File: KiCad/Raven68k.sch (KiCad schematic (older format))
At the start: 22 parts, among them CON1 BARREL_JACK, P1 CONN_01X06, U1 68000D, U2 28C256, U3 SRAM_512Ko, U4 SRAM_512Ko, U5 28C256, U6 XC9572XL-TQ100, U7 68681, Y1 Crystal_GND24

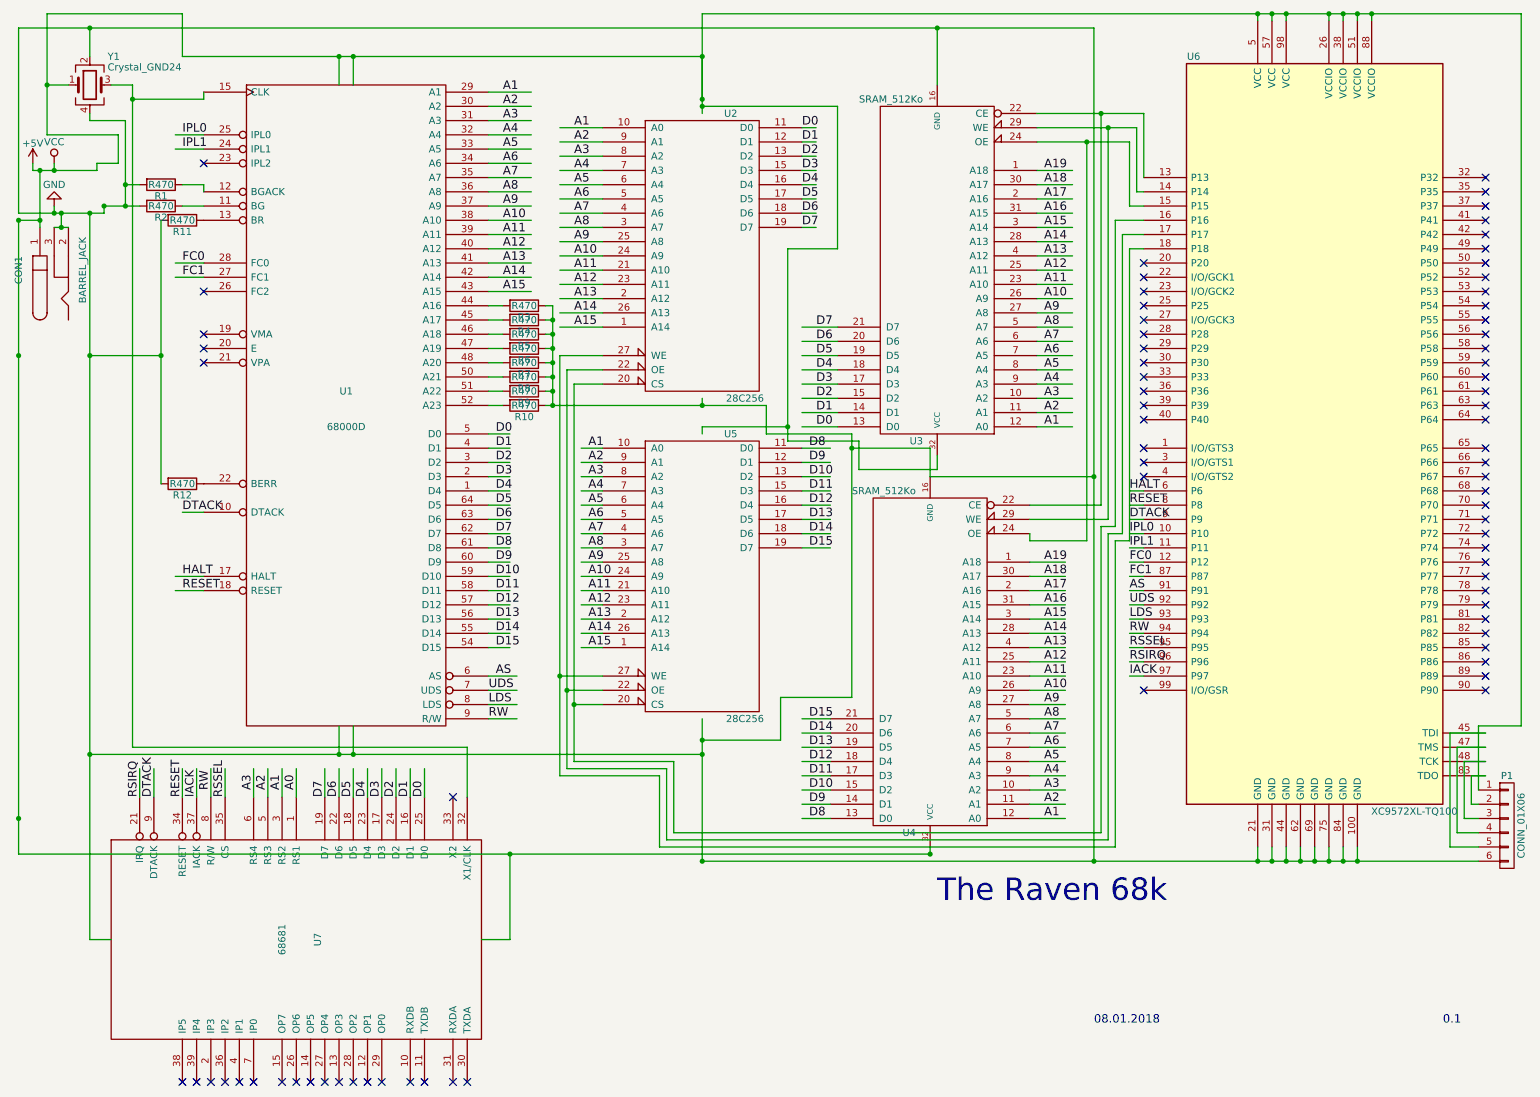
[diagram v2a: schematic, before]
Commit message: Fixed an issue with un-connected address pins a16..a19 and wrong address pin numbering on the RSx register select pins on the 68681.
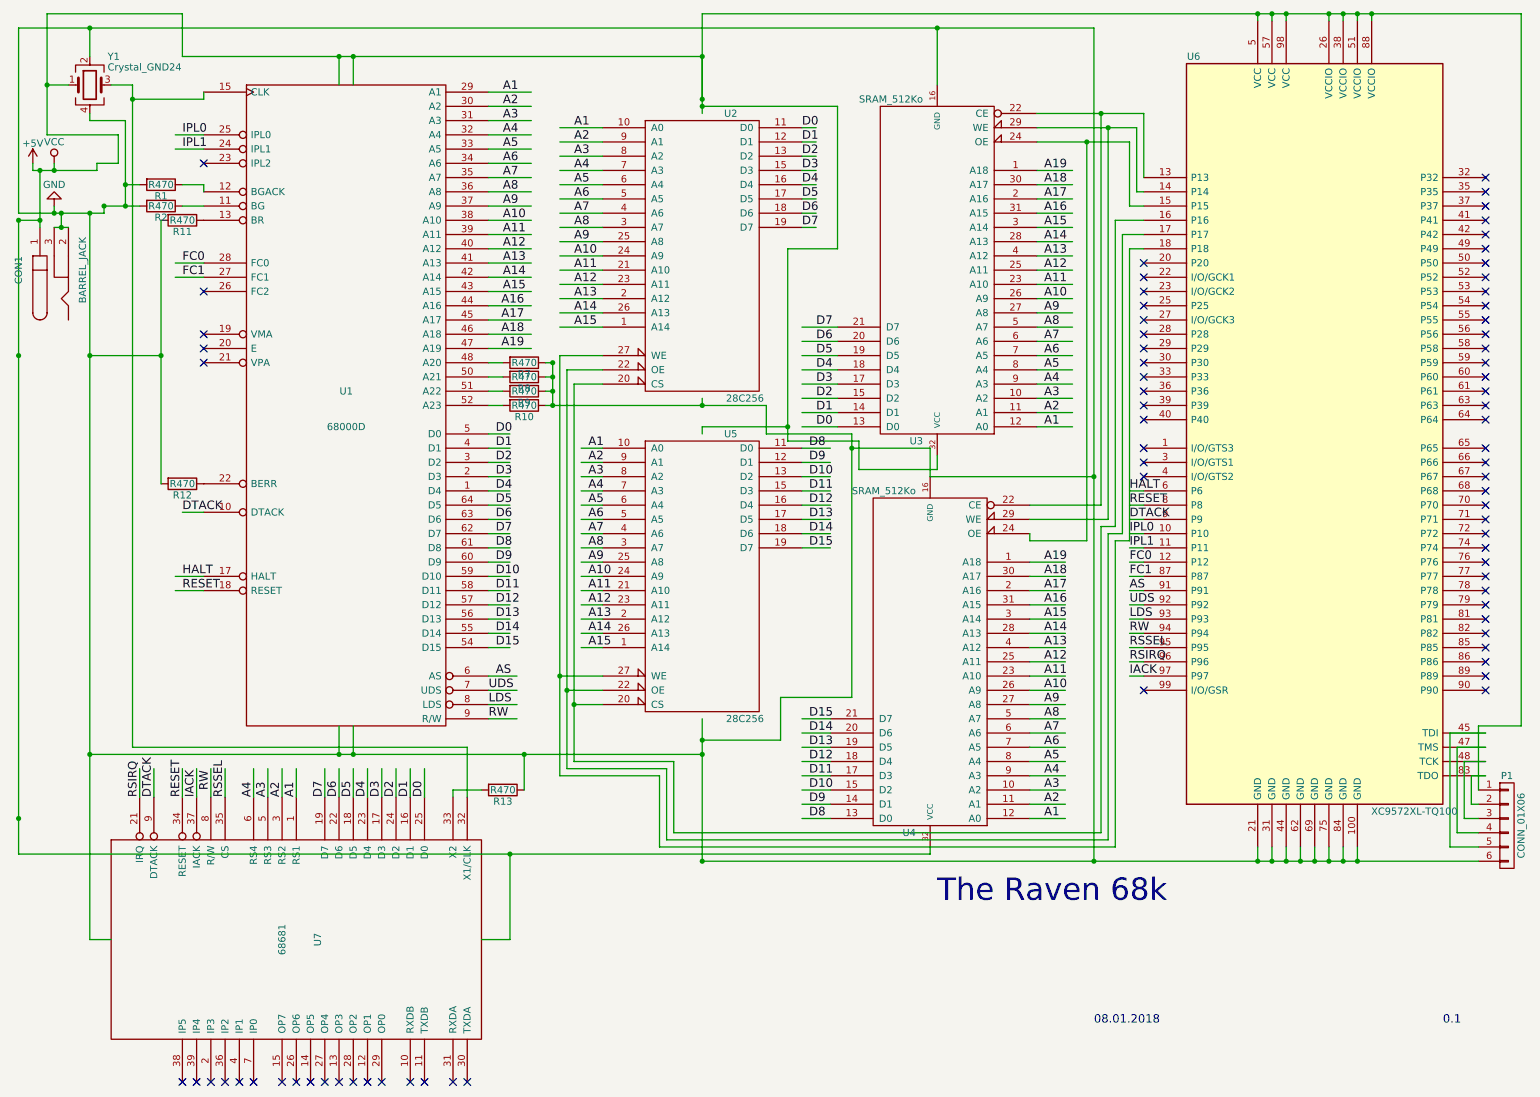
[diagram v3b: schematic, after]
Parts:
- removed R3, R4, R5, R6: R470, Resistors_Universal:Resistor_SMD+THTuniversal_1206_RM10_HandSoldering, symbol R
- added R13: R470, Resistors_Universal:Resistor_SMD+THTuniversal_1206_RM10_HandSoldering, symbol R
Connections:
- net labels removed: A0
- wire segments 343 -> 342
- no-connect marks 76 -> 75
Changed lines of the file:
@@
 FC1
-$Comp
-L R R3
-U 1 1 5A56B70B
-P 4150 2600
-F 0 "R3" V 4230 2600 50  0000 C CNN
-F 1 "R470" V 4150 2600 50  0000 C CNN
-F 2 "Resistors_Universal:Resistor_SMD+THTuniversal_1206_RM10_HandSoldering" V 4080 2600 50  0001 C CNN
-F 3 "" H 4150 2600 50  0000 C CNN
-	1    4150 2600
-	0    1    1    0
-$EndComp
-$Comp
-L R R4
-U 1 1 5A56B7AF
-P 4150 2700
-F 0 "R4" V 4230 2700 50  0000 C CNN
-F 1 "R470" V 4150 2700 50  0000 C CNN
-F 2 "Resistors_Universal:Resistor_SMD+THTuniversal_1206_RM10_HandSoldering" V 4080 2700 50  0001 C CNN
-F 3 "" H 4150 2700 50  0000 C CNN
-	1    4150 2700
-	0    1    1    0
-$EndComp
-$Comp
-L R R5
-U 1 1 5A56B7E6
-P 4150 2800
-F 0 "R5" V 4230 2800 50  0000 C CNN
-F 1 "R470" V 4150 2800 50  0000 C CNN
-F 2 "Resistors_Universal:Resistor_SMD+THTuniversal_1206_RM10_HandSoldering" V 4080 2800 50  0001 C CNN
-F 3 "" H 4150 2800 50  0000 C CNN
-	1    4150 2800
-	0    1    1    0
-$EndComp
-$Comp
-L R R6
-U 1 1 5A56B820
-P 4150 2900
-F 0 "R6" V 4230 2900 50  0000 C CNN
-F 1 "R470" V 4150 2900 50  0000 C CNN
-F 2 "Resistors_Universal:Resistor_SMD+THTuniversal_1206_RM10_HandSoldering" V 4080 2900 50  0001 C CNN
-F 3 "" H 4150 2900 50  0000 C CNN
-	1    4150 2900
-	0    1    1    0
-$EndComp
 $Comp
 L R R7
@@
 	1750 850  5400 850
 Wire Wire Line
-	2950 5750 2950 5550
-Connection ~ 2950 5750
-Wire Wire Line
 	5400 850  5400 1250
 Connection ~ 600  6200
@@
 	600  2000 600  6450
 Wire Wire Line
-	7000 6400 7000 6450
-Connection ~ 7000 6450
-Wire Wire Line
 	9900 6400 9900 6500
 Connection ~ 9900 6500
@@
 	9400 600  9400 550
 Connection ~ 9400 550
-Wire Wire Line
-	9300 600  9300 550
-Connection ~ 9300 550
 Wire Wire Line
 	10100 550  10100 600
@@
 	8500 4500 8400 4500
 Wire Wire Line
-	3900 2600 4000 2600
-Wire Wire Line
-	3900 2700 4000 2700
-Wire Wire Line
-	3900 2800 4000 2800
-Wire Wire Line
-	3900 2900 4000 2900
-Wire Wire Line
 	3900 3000 4000 3000
 Wire Wire Line
@@
 	3900 3300 4000 3300
 Wire Wire Line
-	4300 2600 4350 2600
-Wire Wire Line
 	4350 3200 4300 3200
 Wire Wire Line
@@
 	4350 3000 4300 3000
 Wire Wire Line
-	4350 2900 4300 2900
-Wire Wire Line
-	4350 2800 4300 2800
-Wire Wire Line
-	4300 2700 4350 2700
-Wire Wire Line
 	7700 4700 7950 4700
-Wire Wire Line
-	4350 2600 4350 3300
-Connection ~ 4350 2700
-Connection ~ 4350 2800
-Connection ~ 4350 2900
 Connection ~ 4350 3000
 Connection ~ 4350 3100
@@
 Connection ~ 8150 6500
 Wire Wire Line
-	7000 6450 600  6450
+	600  6450 7000 6450
 Wire Wire Line
 	5400 5500 5400 6500
@@
 Connection ~ 2850 5750
 Wire Wire Line
-	5400 3250 5400 3300
-Connection ~ 5400 3300
-Wire Wire Line
 	5400 3450 5400 3500
 Wire Wire Line
@@
 Wire Wire Line
 	6500 3750 7050 3750
-Wire Wire Line
-	7050 3750 7050 3650
 Wire Wire Line
 	850  1600 850  1650
@@
 Wire Wire Line
 	2250 6050 2250 5850
-Text Label 2550 6000 1    60   ~ 0
-A0
-Text Label 2450 6000 1    60   ~ 0
-A1
-Text Label 2350 6000 1    60   ~ 0
-A2
-Text Label 2250 6000 1    60   ~ 0
-A3
 Connection ~ 5400 6500
 Connection ~ 5400 5750
@@
 	3750 5700 3750 6050
 Connection ~ 1400 1150
-NoConn ~ 3650 6050
+$Comp
+L R R13
+U 1 1 5A5921D0
+P 4000 6000
+F 0 "R13" V 4080 6000 50  0000 C CNN
+F 1 "R470" V 4000 6000 50  0000 C CNN
+F 2 "Resistors_Universal:Resistor_SMD+THTuniversal_1206_RM10_HandSoldering" V 3930 6000 50  0001 C CNN
+F 3 "" H 4000 6000 50  0000 C CNN
+	1    4000 6000
+	0    1    1    0
+$EndComp
+Wire Wire Line
+	3650 6050 3650 6000
+Wire Wire Line
+	3650 6000 3850 6000
+Wire Wire Line
+	4150 6000 4150 5750
+Connection ~ 4150 5750
+Wire Wire Line
+	4350 3000 4350 3300
+Wire Wire Line
+	3900 2600 4200 2600
+Wire Wire Line
+	3900 2700 4200 2700
+Wire Wire Line
+	3900 2800 4200 2800
+Wire Wire Line
+	3900 2900 4200 2900
+Text Label 4150 2600 2    60   ~ 0
+A16
+Text Label 4150 2700 2    60   ~ 0
+A17
+Text Label 4150 2800 2    60   ~ 0
+A18
+Text Label 4150 2900 2    60   ~ 0
+A19
+Text Label 2550 6050 1    60   ~ 0
+A1
+Text Label 2450 6050 1    60   ~ 0
+A2
+Text Label 2350 6050 1    60   ~ 0
+A3
+Text Label 2250 6050 1    60   ~ 0
+A4
+Wire Wire Line
+	7050 3750 7050 3650
+Wire Wire Line
+	7000 6450 7000 6400
+Wire Wire Line
+	2950 5550 2950 5750
+Connection ~ 2950 5750
+Wire Wire Line
+	9300 600  9300 550
+Connection ~ 9300 550
+Wire Wire Line
+	5400 3250 5400 3300
+Connection ~ 5400 3300
 $EndSCHEMATC

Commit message: hierarchial sheets
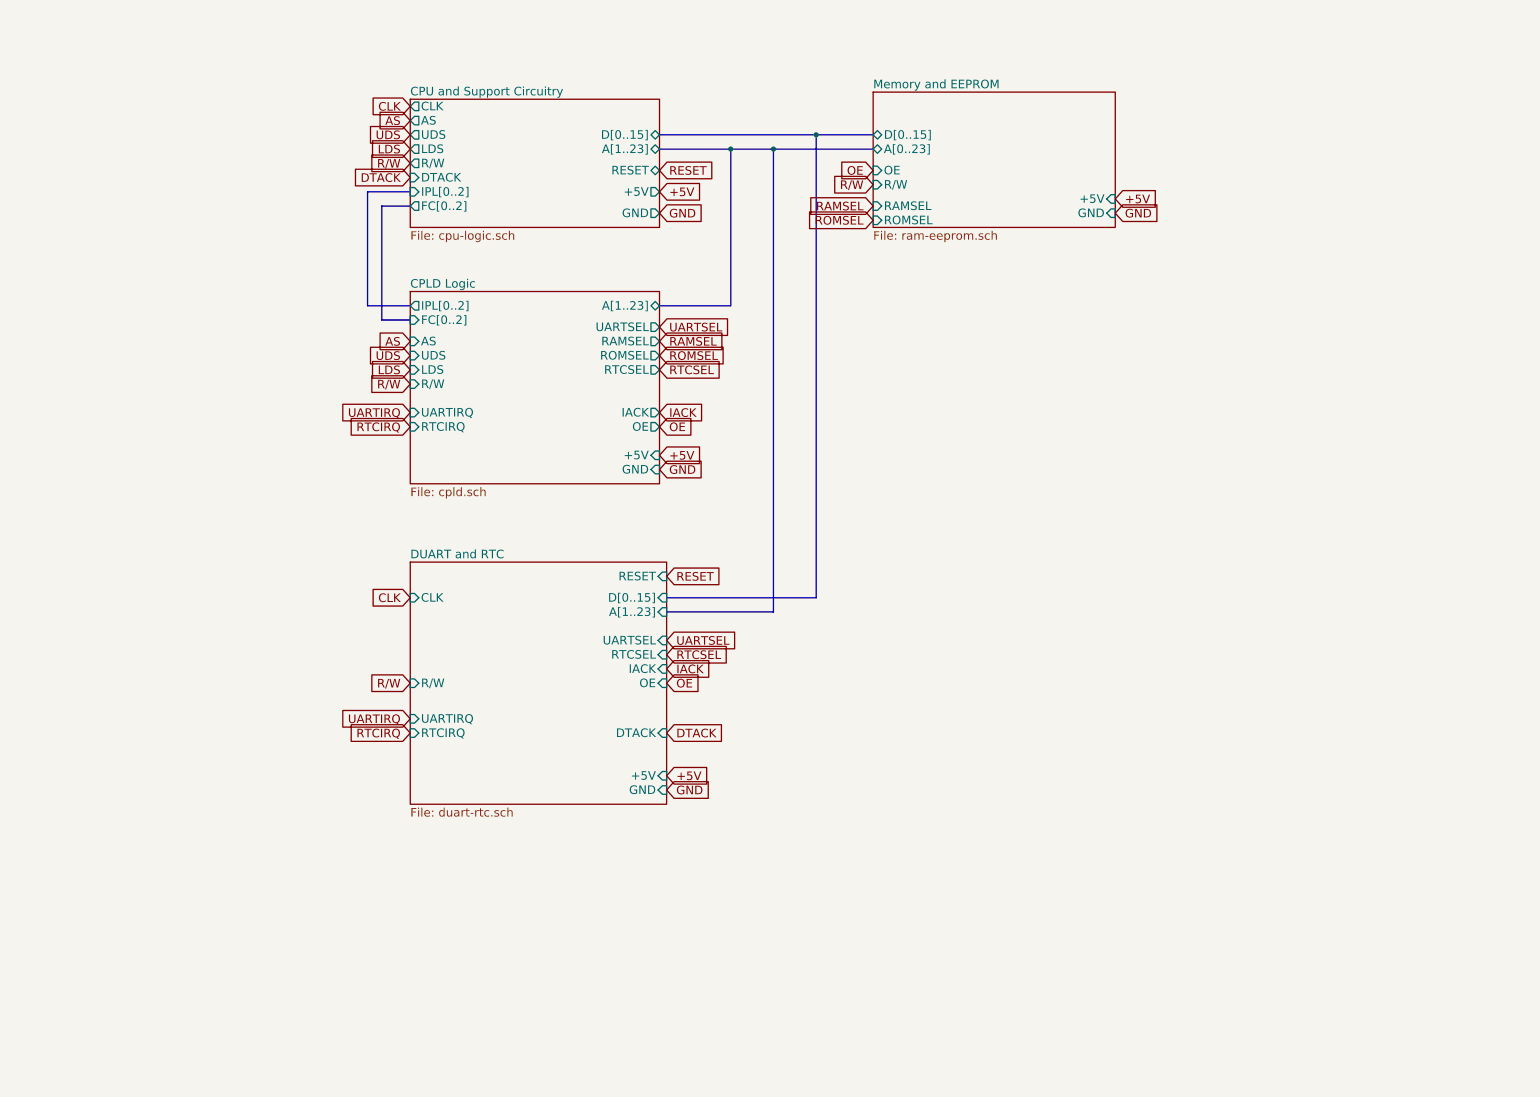
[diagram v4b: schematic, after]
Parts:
- removed CON1: BARREL_JACK, symbol BARREL_JACK
- removed P1: CONN_01X06, symbol CONN_01X06
- removed R1, R10, R11, R12, R13, R2, R7, R8, R9: R470, Resistors_Universal:Resistor_SMD+THTuniversal_1206_RM10_HandSoldering, symbol R
- removed U1: 68000D, Housings_DIP:DIP-64_W22.86mm, symbol 68000D
- removed U2, U5: 28C256, Housings_DIP:DIP-28_W15.24mm, symbol 28C256
- removed U3, U4: SRAM_512Ko, Housings_DIP:DIP-32_W15.24mm, symbol SRAM_512Ko
- removed U6: XC9572XL-TQ100, Housings_QFP:TQFP-100_14x14mm_Pitch0.5mm, symbol XC9572XL-TQ100
- removed U7: 68681, symbol 68681
- removed Y1: Crystal_GND24, Crystals:Crystal_SMD_2520_4Pads, symbol Crystal_GND24
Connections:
- net labels added: CLK, OE, R/W, RAMSEL, ROMSEL, RTCIRQ, RTCSEL, UARTIRQ, UARTSEL
- net labels removed: A1, A10, A11, A12, A13, A14, A15, A16, A17, A18, A19, A2, A3, A4, A5, A6, A7, A8, A9, D0, D1, D10, D11, D12, D13, D14, D15, D2, D3, D4, D5, D6, D7, D8, D9, FC0, FC1, HALT, IPL0, IPL1, RSIRQ, RSSEL, RW, VCC
- wire segments 342 -> 0
- no-connect marks 75 -> 0
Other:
- note removed: "0.1"
- note removed: "08.01.2018"
- note removed: "The Raven 68k"
